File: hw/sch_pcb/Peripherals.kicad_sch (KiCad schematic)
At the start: 45 parts, among them IC2 CY15B108QN-40SXI, IC4 FM3164-S, J17 HEADER_2x03_PARALLEL, J20 MCC-SD, J21 MCC-SD (kouka z modulu), Q2 DMP2045UQ-7, U10 TPS22965-Q1, U12 MS5611-01BA, U8 TXS0108EPW, U9 ICM-20948, Y2 6pF crystal

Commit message: progress?
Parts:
- removed J20: MCC-SD, Connector_Card:SD_TE_2041021, symbol DATALOGGER01A-rescue:SD_Card-Connector
- removed R38: -, Mlab_R:SMD-0603, symbol Device:R
- removed R39: 0R, Mlab_R:SMD-0603, symbol Device:R
- added JP4: SolderJumper_3_Bridged12, Jumper:SolderJumper-3_P1.3mm_Bridged12_RoundedPad1.0x1.5mm_NumberLabels, symbol Jumper:SolderJumper_3_Bridged12
- BT1: renamed from BT2; footprint Mlab_Batery:CH28-2032 -> Battery:BatteryHolder_Keystone_2998_1x6.8mm
- C14: renamed from C31; footprint Mlab_R:SMD-0603 -> Mlab_C:SMD-0805
- C15: renamed from C32; footprint Mlab_R:SMD-0603 -> Mlab_C:SMD-0805
- C16: renamed from C33; footprint Mlab_R:SMD-0603 -> Mlab_C:SMD-0805
- C17: renamed from C34; footprint Mlab_R:SMD-0805 -> Mlab_C:SMD-0805
- C18: renamed from C35; footprint Mlab_R:SMD-0603 -> Mlab_C:SMD-0805
- C19: renamed from C36; footprint Mlab_R:SMD-0603 -> Mlab_C:SMD-0805
- C20: renamed from C37; footprint Mlab_R:SMD-0805 -> Mlab_C:SMD-0805
- C21: renamed from C39; footprint Mlab_R:SMD-0805 -> Mlab_C:SMD-0805
- C22: renamed from C42; footprint (none) -> Mlab_C:SMD-0805
- C23: renamed from C43; footprint Mlab_R:SMD-0805 -> Mlab_C:SMD-0805
- C24: renamed from C73; footprint (none) -> Mlab_C:SMD-0805
- C25: renamed from C44; footprint Mlab_R:SMD-0805 -> Mlab_C:SMD-0805
- D1: renamed from D15; footprint Mlab_D:FIX-LED-313 -> Mlab_D:LED_1206_mill
- IC1: renamed from IC2; footprint SOIC127P800X203-8N -> Mlab_IO:SOIC-8_3.9x4.9mm_Pitch1.27mm
- IC2: renamed from IC4; value FM3164-S -> FM3164-G; footprint SOIC127P600X175-14N -> Mlab_IO:SOIC-14
- R14: renamed from R40; footprint Mlab_R:SMD-0603 -> Mlab_R:SMD-0805
- R15: renamed from R41; footprint Mlab_R:SMD-0603 -> Mlab_R:SMD-0805
- R16: renamed from R42; footprint Mlab_R:SMD-0603 -> Mlab_R:SMD-0805
- R17: renamed from R43; footprint Mlab_R:SMD-0603 -> Mlab_R:SMD-0805
- R18: renamed from R44; footprint (none) -> Mlab_R:SMD-0805
- R19: renamed from R45; footprint (none) -> Mlab_R:SMD-0805
- R20: renamed from R46; footprint (none) -> Mlab_R:SMD-0805
- R21: renamed from R69; footprint (none) -> Mlab_R:SMD-0805
- R22: renamed from R70; footprint (none) -> Mlab_R:SMD-0805
- R23: renamed from R71; footprint (none) -> Mlab_R:SMD-0805
- Y2: value 6pF crystal -> 6pF crystal - 32.768kHz
- renumbered J17 to J4, J21 to J6, JP2 to JP1, JP3 to JP2, JP1 to JP3, Q2 to Q1, R47 to R24, R48 to R25, R49 to R26, R50 to R27, R51 to R28, U8 to U4, U9 to U5, U10 to U6, U12 to U7
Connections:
- net +3V3 is gone; now on net +3.3V: C16.1, C18.1, R18.1, R19.1, U4.19 (VCCB), U5.13 (VDD)
- net VDD is gone; now on net +3.3V: JP1.1 (A), JP2.1 (A), JP3.1 (A)
- net +1V8: now also JP4.1 (A)
- net GND: now also JP4.3 (B)
- net AD0: now reaches U5.9 (SDO/AD0)
- net AD0: now also JP4.2 (C)
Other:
- note removed: "select i2c LSB address"

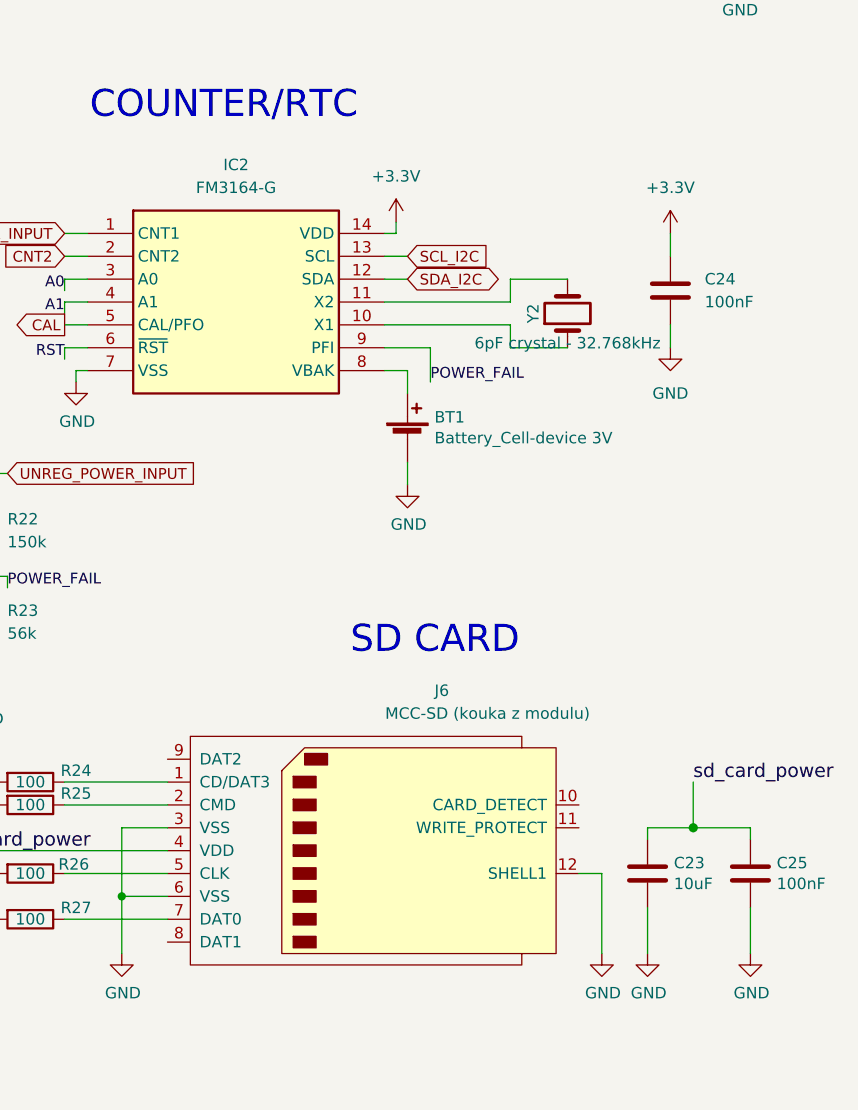
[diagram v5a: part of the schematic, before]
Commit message: Update components from libraries. Improve schematics. Resolve some ERC and DRC errors.
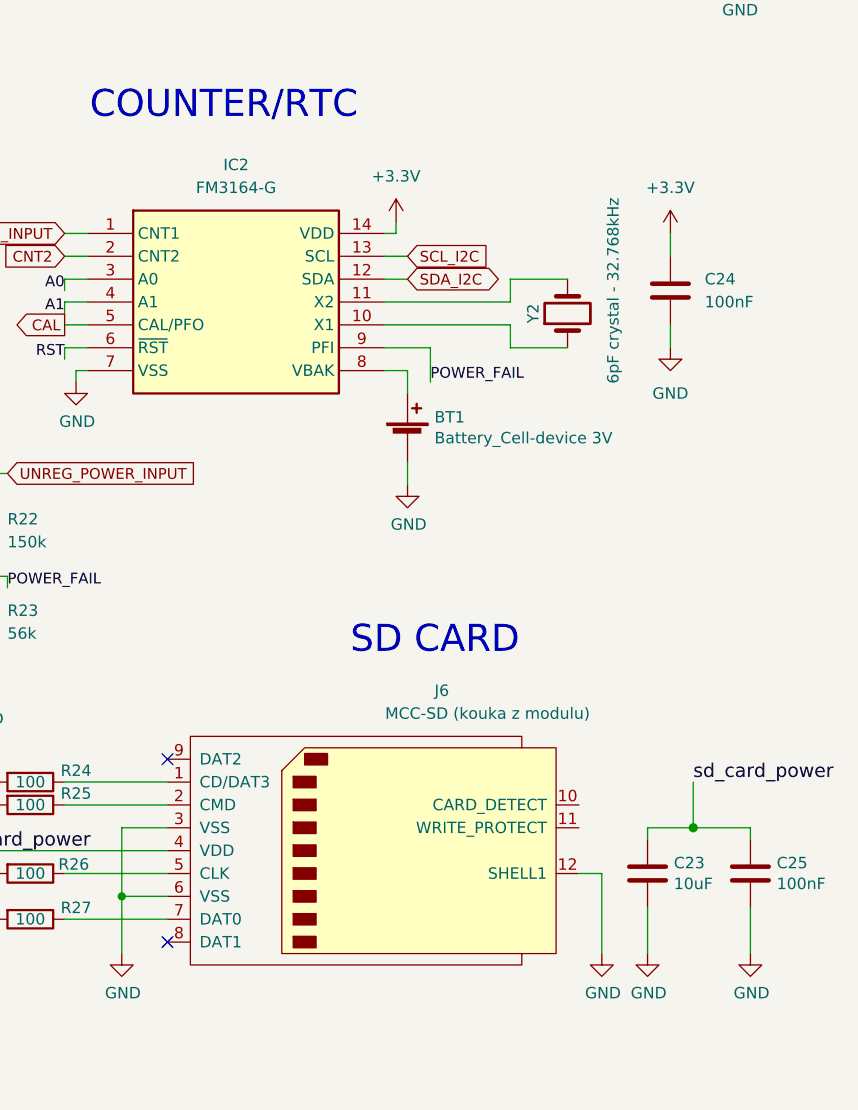
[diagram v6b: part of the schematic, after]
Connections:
- no-connect marks 2 -> 4

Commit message: Update footprints. Improve layout Fix some DRC errors. Set components values matching inventory.
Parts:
- C14, C15, C16, C17, C18, C19, C20, C21, C22, C23, C24, C25: footprint Mlab_C:SMD-0805 -> Capacitor_SMD:C_0805_2012Metric
- IC2: footprint Mlab_IO:SOIC-14 -> Package_SO:SOIC-14_3.9x8.7mm_P1.27mm
- R14, R15, R16, R17, R18, R19, R20, R21, R22, R23, R24, R25, R26, R27, R28: footprint Mlab_R:SMD-0805 -> Resistor_SMD:R_0805_2012Metric
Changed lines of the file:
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@@
 			)
 		)
-		(property "Footprint" "Mlab_IO:SOIC-14"
+		(property "Footprint" "Package_SO:SOIC-14_3.9x8.7mm_P1.27mm"
 			(at 228.6 171.12 0)
 			(effects
@@
 			)
 		)
-		(property "Datasheet" "https://4donline.ihs.com/images/VipMasterIC/IC/RAMT/RAMTS00396/RAMTS00396-1.pdf?hkey=EF798316E3902B6ED9A73243A3159BB0"
+		(property "Datasheet" "https://www.tme.eu/Document/fd7387082c26a47b1cfc6f4ba6bd97fb/FM3164_31256-DTE.pdf"
 			(at 228.6 271.12 0)
 			(effects
@@
 			)
 		)
+		(property "UST_ID" ""
+			(at 199.39 76.2 0)
+			(effects
+				(font
+					(size 1.27 1.27)
+				)
+				(hide yes)
+			)
+		)
 		(pin "9"
 		)
@@
 			)
 		)
-		(property "Footprint" "Mlab_R:SMD-0805"
+		(property "Footprint" "Resistor_SMD:R_0805_2012Metric"
 			(at 92.202 93.98 90)
 			(effects
@@
 			)
 		)
-		(property "Footprint" "Mlab_R:SMD-0805"
+		(property "Footprint" "Resistor_SMD:R_0805_2012Metric"
 			(at 186.182 119.38 90)
 			(effects
@@
 			)
 		)
-		(property "Footprint" "Mlab_R:SMD-0805"
+		(property "Footprint" "Resistor_SMD:R_0805_2012Metric"
 			(at 273.558 31.75 90)
 			(effects
@@
 			)
 		)
-		(property "Footprint" "Mlab_C:SMD-0805"
+		(property "Footprint" "Capacitor_SMD:C_0805_2012Metric"
 			(at 93.6752 40.64 0)
 			(effects
@@
 			)
 		)
-		(property "Footprint" "Mlab_C:SMD-0805"
+		(property "Footprint" "Capacitor_SMD:C_0805_2012Metric"
 			(at 274.0152 151.13 0)
 			(effects
@@
 			)
 		)
-		(property "Footprint" "Mlab_C:SMD-0805"
+		(property "Footprint" "Capacitor_SMD:C_0805_2012Metric"
 			(at 265.1252 86.36 0)
 			(effects
@@
 			)
 		)
-		(property "Footprint" "Mlab_R:SMD-0805"
+		(property "Footprint" "Resistor_SMD:R_0805_2012Metric"
 			(at 193.04 135.382 90)
 			(effects
@@
 			)
 		)
-		(property "Footprint" "Mlab_R:SMD-0805"
+		(property "Footprint" "Resistor_SMD:R_0805_2012Metric"
 			(at 111.252 157.48 90)
 			(effects
@@
 			)
 		)
-		(property "Footprint" "Mlab_C:SMD-0805"
+		(property "Footprint" "Capacitor_SMD:C_0805_2012Metric"
 			(at 68.2752 152.4 0)
 			(effects
@@
 			)
 		)
-		(property "Footprint" "Mlab_R:SMD-0805"
+		(property "Footprint" "Resistor_SMD:R_0805_2012Metric"
 			(at 193.04 137.922 90)
 			(effects
@@
 			)
 		)
-		(property "Footprint" "Mlab_C:SMD-0805"
+		(property "Footprint" "Capacitor_SMD:C_0805_2012Metric"
 			(at 92.4052 120.65 0)
 			(effects
@@
 			)
 		)
-		(property "Footprint" "Mlab_R:SMD-0805"
+		(property "Footprint" "Resistor_SMD:R_0805_2012Metric"
 			(at 193.04 145.542 90)
 			(effects
@@
 			)
 		)
-		(property "Footprint" "Mlab_C:SMD-0805"
+		(property "Footprint" "Capacitor_SMD:C_0805_2012Metric"
 			(at 63.1952 83.82 0)
 			(effects
@@
 			)
 		)
-		(property "Footprint" "Mlab_R:SMD-0805"
+		(property "Footprint" "Resistor_SMD:R_0805_2012Metric"
 			(at 160.782 158.75 90)
 			(effects
@@
 			)
 		)
-		(property "Footprint" "Mlab_R:SMD-0805"
+		(property "Footprint" "Resistor_SMD:R_0805_2012Metric"
 			(at 21.082 93.98 90)
 			(effects
@@
 			)
 		)
-		(property "Footprint" "Mlab_C:SMD-0805"
+		(property "Footprint" "Capacitor_SMD:C_0805_2012Metric"
 			(at 73.3552 39.37 0)
 			(effects
@@
 			)
 		)
-		(property "Footprint" "Mlab_C:SMD-0805"
+		(property "Footprint" "Capacitor_SMD:C_0805_2012Metric"
 			(at 39.6748 144.78 0)
 			(effects
@@
 			)
 		)
-		(property "Footprint" "Mlab_C:SMD-0805"
+		(property "Footprint" "Capacitor_SMD:C_0805_2012Metric"
 			(at 83.5152 83.82 0)
 			(effects
@@
 			)
 		)
-		(property "Footprint" "Mlab_R:SMD-0805"
+		(property "Footprint" "Resistor_SMD:R_0805_2012Metric"
 			(at 27.432 93.98 90)
 			(effects
@@
 			)
 		)
-		(property "Footprint" "Mlab_R:SMD-0805"
+		(property "Footprint" "Resistor_SMD:R_0805_2012Metric"
 			(at 102.362 157.48 90)
 			(effects
@@
 			)
 		)
-		(property "Footprint" "Mlab_R:SMD-0805"
+		(property "Footprint" "Resistor_SMD:R_0805_2012Metric"
 			(at 172.212 93.98 90)
 			(effects
@@
 			)
 		)
-		(property "Footprint" "Mlab_R:SMD-0805"
+		(property "Footprint" "Resistor_SMD:R_0805_2012Metric"
 			(at 186.182 109.22 90)
 			(effects
@@
 			)
 		)
-		(property "Footprint" "Mlab_C:SMD-0805"
+		(property "Footprint" "Capacitor_SMD:C_0805_2012Metric"
 			(at 262.5852 151.13 0)
 			(effects
@@
 			)
 		)
-		(property "Footprint" "Mlab_C:SMD-0805"
+		(property "Footprint" "Capacitor_SMD:C_0805_2012Metric"
 			(at 234.6452 40.64 0)
 			(effects
@@
 			)
 		)
-		(property "Footprint" "Mlab_R:SMD-0805"
+		(property "Footprint" "Resistor_SMD:R_0805_2012Metric"
 			(at 98.552 93.98 90)
 			(effects
@@
 			)
 		)
-		(property "Footprint" "Mlab_R:SMD-0805"
+		(property "Footprint" "Resistor_SMD:R_0805_2012Metric"
 			(at 193.04 150.622 90)
 			(effects
@@
 			)
 		)
-		(property "Footprint" "Mlab_C:SMD-0805"
+		(property "Footprint" "Capacitor_SMD:C_0805_2012Metric"
 			(at 126.6952 39.37 0)
 			(effects
